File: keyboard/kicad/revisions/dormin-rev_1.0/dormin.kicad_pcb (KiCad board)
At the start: 2 copper layers, 141.5 x 103.1 mm, 24 parts

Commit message: feat: clean pcb and outline
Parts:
- added SW1: SW_Push, willkeebs_keyboard:SW_MX_Choc_Hotswap, F.Cu at (89.0, 76.8)
- added U3: XIAO-nRF52840-Plus-SMD, Seeed_Studio_XIAO_Series:XIAO-nRF52840-Plus-SMD, B.Cu at (194.0, 105.2)
- SW1: renamed from S6; value (none) -> SW_Push
- moved D23 68.7 mm to (78.8, 102.0)
- moved D24 68.7 mm to (83.4, 102.0)
- moved SW1 68.7 mm to (95.5, 105.3)
- moved SW11 68.7 mm to (95.5, 143.4)
- moved SW13 68.7 mm to (133.6, 133.9)
- moved SW14 68.7 mm to (152.6, 138.6)
- moved SW18 68.7 mm to (150.7, 163.4)
- moved SW3 68.7 mm to (133.6, 95.8)
- moved SW4 68.7 mm to (152.6, 100.5)
- moved SW6 68.7 mm to (95.5, 124.3)
- moved SW8 68.7 mm to (133.6, 114.8)
- moved SW9 68.7 mm to (152.6, 119.6)
- moved D21 68.7 mm to (69.4, 102.0)
- moved D22 68.7 mm to (74.1, 101.9)
- moved SW16 68.7 mm to (76.4, 114.8)
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- renumbered S17 to SW10, S4 to SW11, S7 to SW12, S10 to SW13, S13 to SW14, S16 to SW15, S3 to SW16, S2 to SW17, S19 to SW18, S20 to SW19, S9 to SW2, S21 to SW20, S12 to SW3, S15 to SW4, S18 to SW5, S5 to SW6, S8 to SW7, S11 to SW8, S14 to SW9
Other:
- outline, holes or cut-outs redrawn

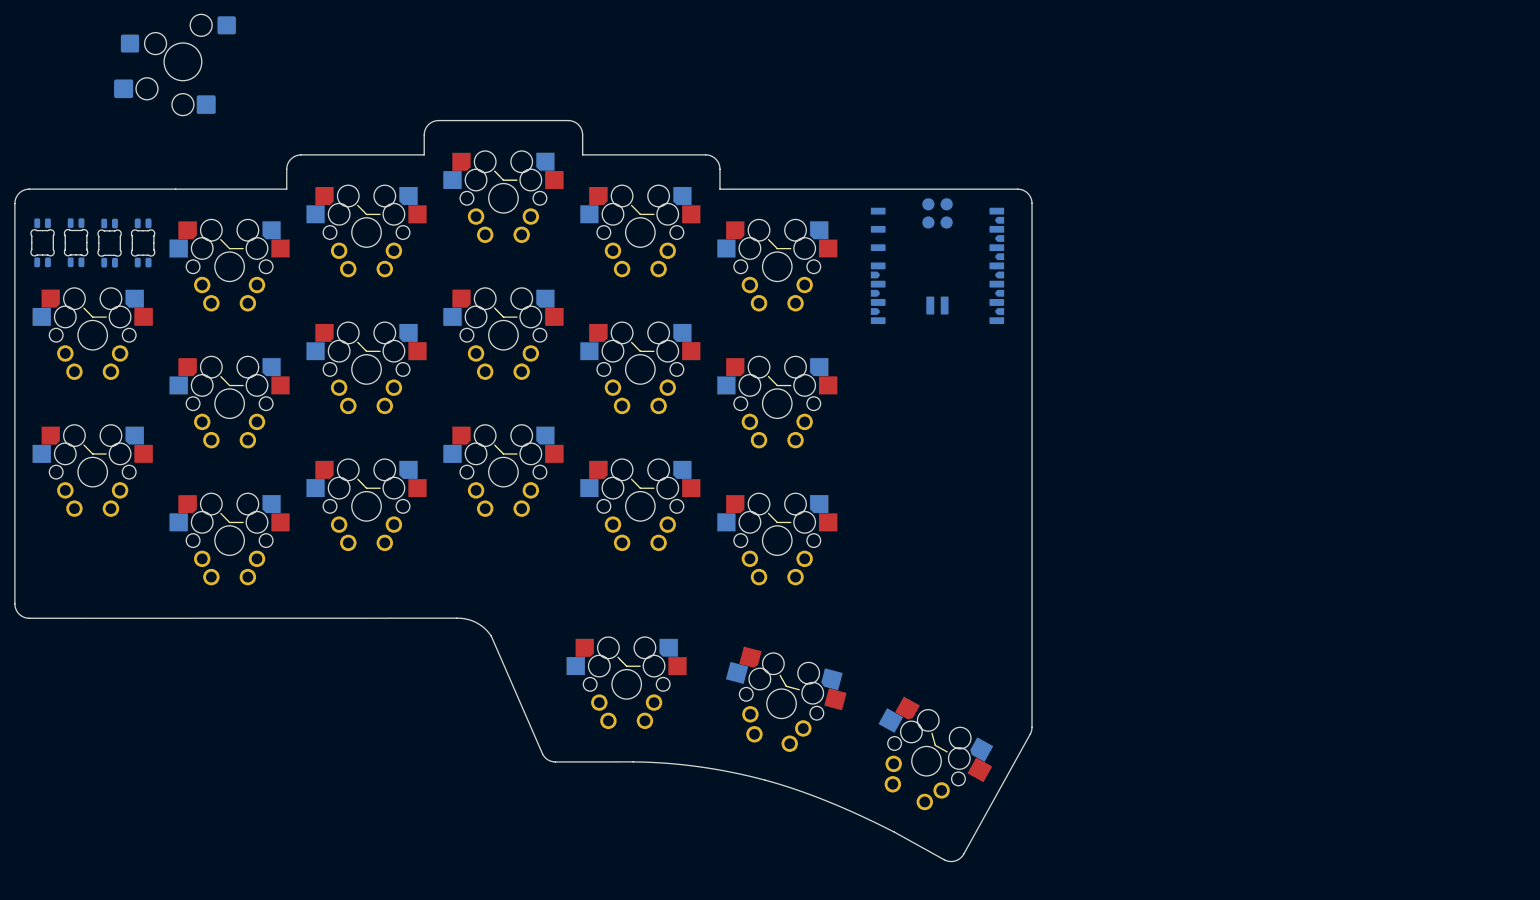
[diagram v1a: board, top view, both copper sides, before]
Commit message: feat: start PCB placement
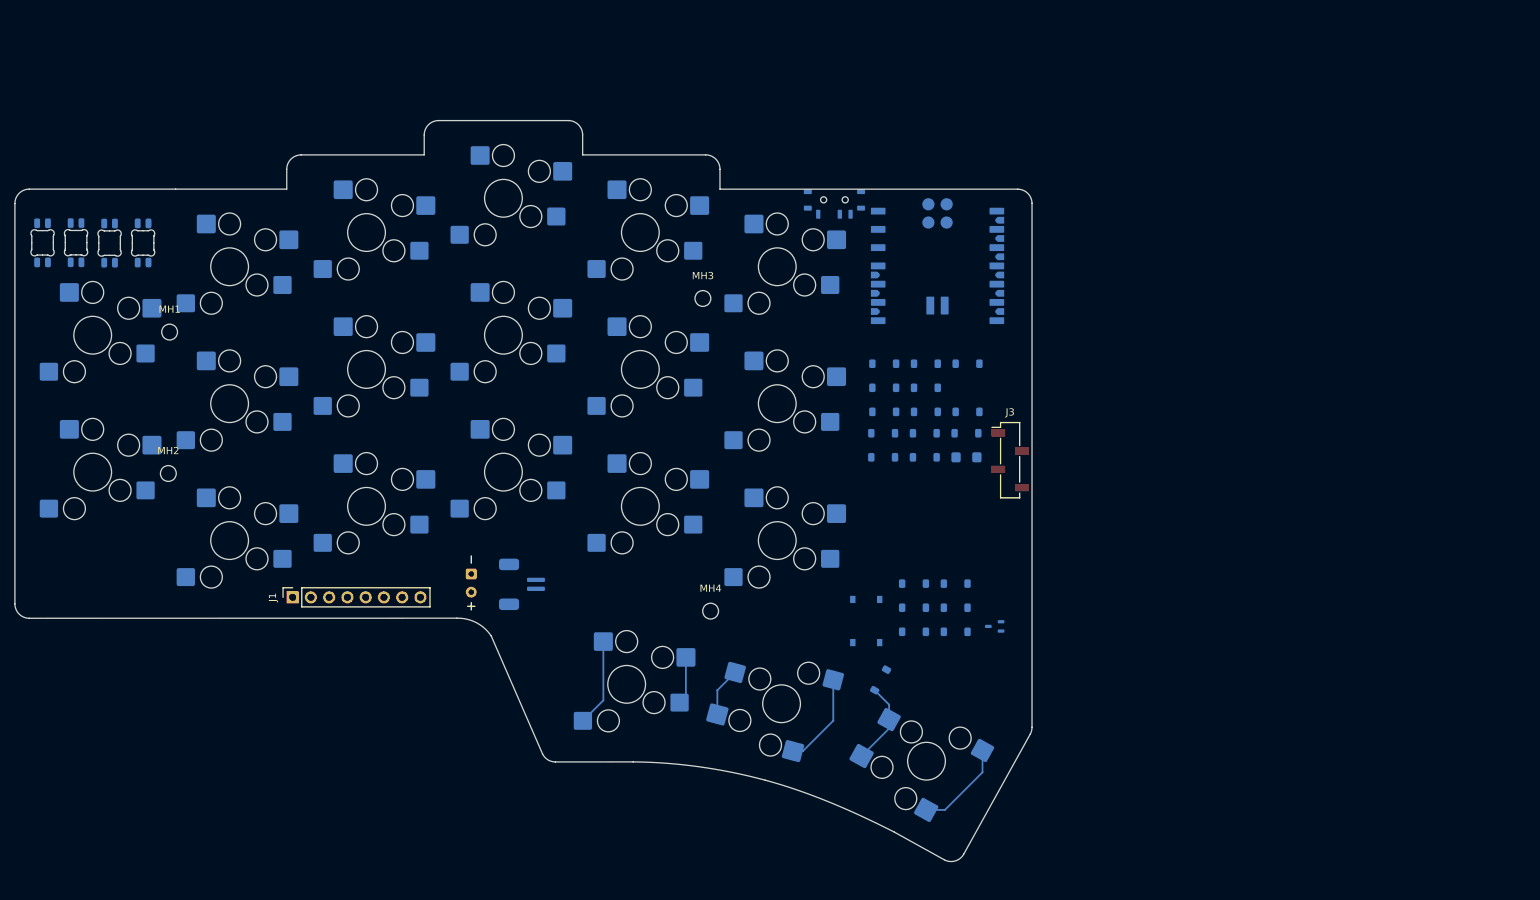
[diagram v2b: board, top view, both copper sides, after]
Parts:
- removed the SW1 at (89.0, 76.8)
- added BT1: Pads, willkeebs_power:Battery_Pad, F.Cu at (129.1, 149.3)
- added D1: 1N4148W, Diode_SMD:D_SOD-123, B.Cu at (186.6, 118.8)
- added D10: 1N4148W, Diode_SMD:D_SOD-123, B.Cu at (192.3, 122.1)
- added D11: 1N4148W, Diode_SMD:D_SOD-123, B.Cu at (192.3, 125.5)
- added D12: 1N4148W, Diode_SMD:D_SOD-123, B.Cu at (192.2, 128.4)
- added D13: 1N4148W, Diode_SMD:D_SOD-123, B.Cu at (192.2, 131.8)
- added D14: 1N4148W, Diode_SMD:D_SOD-123, B.Cu at (196.5, 149.4)
- added D15: 1N4148W, Diode_SMD:D_SOD-123, B.Cu at (196.5, 152.7)
- added D16: 1N4148W, Diode_SMD:D_SOD-123, B.Cu at (196.5, 156.1)
- added D17: 1N4148W, Diode_SMD:D_SOD-123, B.Cu at (198.1, 118.8)
- added D18: 1N4148W, Diode_SMD:D_SOD-123, B.Cu at (186.1, 162.8)
- added D19: 1N4148W, Diode_SMD:D_SOD-123, B.Cu at (198.1, 125.5)
- added D2: 1N4148W, Diode_SMD:D_SOD-123, B.Cu at (186.6, 122.1)
- added D20: 1N4148W, Diode_SMD:D_SOD-123, B.Cu at (198.0, 128.4)
- added D28: SMF5V0A, Diode_SMD:D_SMF, B.Cu at (198.0, 131.8)
- added D3: 1N4148W, Diode_SMD:D_SOD-123, B.Cu at (186.6, 125.5)
- added D4: 1N4148W, Diode_SMD:D_SOD-123, B.Cu at (186.4, 128.4)
- added D5: 1N4148W, Diode_SMD:D_SOD-123, B.Cu at (186.4, 131.8)
- added D6: 1N4148W, Diode_SMD:D_SOD-123, B.Cu at (190.7, 149.4)
- added D7: 1N4148W, Diode_SMD:D_SOD-123, B.Cu at (190.7, 152.7)
- added D8: 1N4148W, Diode_SMD:D_SOD-123, B.Cu at (190.7, 156.1)
- added D9: 1N4148W, Diode_SMD:D_SOD-123, B.Cu at (192.3, 118.8)
- added J1: Conn_01x08_Socket, Connector_PinSocket_2.54mm:PinSocket_1x08_P2.54mm_Vertical, F.Cu at (104.2, 151.3)
- added J3: Pogo Connector, Connector_PinSocket_2.54mm:PinSocket_1x04_P2.54mm_Vertical_SMD_Pin1Left, F.Cu at (204.1, 132.2)
- added JST1: Conn_01x02_Pin, willkeebs_power:JST_1.25mm, B.Cu at (135.6, 149.5)
- added MH1: MountingHole_2.2mm_M2, MountingHole:MountingHole_2.2mm_M2, F.Cu at (87.1, 114.4)
- added MH2: MountingHole_2.2mm_M2, MountingHole:MountingHole_2.2mm_M2, F.Cu at (87.0, 134.1)
- added MH3: MountingHole_2.2mm_M2, MountingHole:MountingHole_2.2mm_M2, F.Cu at (161.3, 109.7)
- added MH4: MountingHole_2.2mm_M2, MountingHole:MountingHole_2.2mm_M2, F.Cu at (162.4, 153.2)
- added PSW1: SW_SPDT, willkeebs_power:Switch_MSK12C02, B.Cu at (179.6, 96.0)
- added RSW1: SW_Push, willkeebs_components:SW_Push_1P1T_XKB_TS-1187A, B.Cu at (184.1, 154.6)
- added U4: TPD2E2U06DCK, Package_TO_SOT_SMD:SOT-323_SC-70, B.Cu at (201.9, 155.3)
- SW1: renamed from SW5; value (none) -> SW_Push; footprint ceoloide:switch_mx -> willkeebs_keyboard:SW_MX_Choc_Hotswap; moved to F.Cu
- SW10: renamed from SW6; value (none) -> SW_Push; footprint ceoloide:switch_mx -> willkeebs_keyboard:SW_MX_Choc_Hotswap; moved to F.Cu
- SW11: renamed from SW16; value (none) -> SW_Push; footprint ceoloide:switch_mx -> willkeebs_keyboard:SW_MX_Choc_Hotswap; moved to F.Cu
- SW12: renamed from SW15; value (none) -> SW_Push; footprint ceoloide:switch_mx -> willkeebs_keyboard:SW_MX_Choc_Hotswap; moved to F.Cu
- SW13: renamed from SW14; value (none) -> SW_Push; footprint ceoloide:switch_mx -> willkeebs_keyboard:SW_MX_Choc_Hotswap; moved to F.Cu
- SW14: renamed from SW13; value (none) -> SW_Push; footprint ceoloide:switch_mx -> willkeebs_keyboard:SW_MX_Choc_Hotswap; moved to F.Cu
- SW15: renamed from SW12; value (none) -> SW_Push; footprint ceoloide:switch_mx -> willkeebs_keyboard:SW_MX_Choc_Hotswap; moved to F.Cu
- SW16: renamed from SW11; value (none) -> SW_Push; footprint ceoloide:switch_mx -> willkeebs_keyboard:SW_MX_Choc_Hotswap; moved to F.Cu
- SW17, SW19, SW3, SW8: value (none) -> SW_Push; footprint ceoloide:switch_mx -> willkeebs_keyboard:SW_MX_Choc_Hotswap; moved to F.Cu
- SW18: renamed from SW20; value (none) -> SW_Push; footprint ceoloide:switch_mx -> willkeebs_keyboard:SW_MX_Choc_Hotswap; moved to F.Cu
- SW2: renamed from SW4; value (none) -> SW_Push; footprint ceoloide:switch_mx -> willkeebs_keyboard:SW_MX_Choc_Hotswap; moved to F.Cu
- SW20: renamed from SW18; value (none) -> SW_Push; footprint ceoloide:switch_mx -> willkeebs_keyboard:SW_MX_Choc_Hotswap; moved to F.Cu
- SW4: renamed from SW2; value (none) -> SW_Push; footprint ceoloide:switch_mx -> willkeebs_keyboard:SW_MX_Choc_Hotswap; moved to F.Cu
- SW5: renamed from SW1; footprint ceoloide:switch_mx -> willkeebs_keyboard:SW_MX_Choc_Hotswap; moved to F.Cu
- SW6: renamed from SW10; value (none) -> SW_Push; footprint ceoloide:switch_mx -> willkeebs_keyboard:SW_MX_Choc_Hotswap; moved to F.Cu
- SW7: renamed from SW9; value (none) -> SW_Push; footprint ceoloide:switch_mx -> willkeebs_keyboard:SW_MX_Choc_Hotswap; moved to F.Cu
- SW9: renamed from SW7; value (none) -> SW_Push; footprint ceoloide:switch_mx -> willkeebs_keyboard:SW_MX_Choc_Hotswap; moved to F.Cu
- turned SW1 to 180 degrees
- turned SW10 to 180 degrees
- turned SW11 to 180 degrees
- turned SW12 to 180 degrees
- turned SW13 to 180 degrees
- turned SW14 to 180 degrees
- turned SW15 to 180 degrees
- turned SW16 to 180 degrees
- turned SW17 to 180 degrees
- turned SW2 to 180 degrees
- turned SW20 to 180 degrees
- turned SW3 to 180 degrees
- turned SW4 to 180 degrees
- turned SW5 to 180 degrees
- turned SW6 to 180 degrees
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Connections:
- SW1 pad 1: (no net) -> Net-(D1-A)
- SW1 pad 2: inner_top_sw -> COL5
- SW10 pad 1: (no net) -> Net-(D10-A)
- SW10 pad 2: pinky_home_sw -> COL1
- SW11 pad 1: (no net) -> Net-(D11-A)
- SW11 pad 2: outer_top_sw -> COL0
- SW12 pad 1: (no net) -> Net-(D12-A)
- SW12 pad 2: inner_bottom_sw -> COL5
- SW13 pad 1: (no net) -> Net-(D13-A)
- SW13 pad 2: index_bottom_sw -> COL4
- SW14 pad 1: (no net) -> Net-(D14-A)
- SW14 pad 2: middle_bottom_sw -> COL3
- SW15 pad 1: (no net) -> Net-(D15-A)
- SW15 pad 2: ring_bottom_sw -> COL2
- SW16 pad 1: (no net) -> Net-(D16-A)
- SW16 pad 2: pinky_bottom_sw -> COL1
- SW17 pad 1: (no net) -> Net-(D17-A)
- SW17 pad 2: outer_home_sw -> COL0
- SW18 pad 1: (no net) -> Net-(D18-A)
- SW18 pad 2: outer_only_sw -> COL5
- SW19 pad 1: (no net) -> Net-(D19-A)
- SW19 pad 2: home_only_sw -> COL4
- SW2 pad 1: (no net) -> Net-(D2-A)
- SW2 pad 2: index_top_sw -> COL4
- SW20 pad 1: (no net) -> Net-(D20-A)
- SW20 pad 2: inner_only_sw -> COL3
- SW3 pad 1: (no net) -> Net-(D3-A)
- SW3 pad 2: middle_top_sw -> COL3
- SW4 pad 1: (no net) -> Net-(D4-A)
- SW4 pad 2: ring_top_sw -> COL2
- SW5 pad 1: (no net) -> Net-(D5-A)
- SW5 pad 2: pinky_top_sw -> COL1
- SW6 pad 1: (no net) -> Net-(D6-A)
- SW6 pad 2: inner_home_sw -> COL5
- SW7 pad 1: (no net) -> Net-(D7-A)
- SW7 pad 2: index_home_sw -> COL4
- SW8 pad 1: (no net) -> Net-(D8-A)
- SW8 pad 2: middle_home_sw -> COL3
- SW9 pad 1: (no net) -> Net-(D9-A)
- SW9 pad 2: ring_home_sw -> COL2
- U3 pad 19: EXTG -> unconnected-(U3-D15_NFC2-Pad19)
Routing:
- net COL4: track 0.00 -> 13.0 mm
- net COL5: track 0.00 -> 13.0 mm
- net COL3: track 0.00 -> 12.2 mm
- net Net-(D18-A): track 0.00 -> 11.6 mm
- net Net-(D19-A): track 0.00 -> 6.88 mm
- net Net-(D20-A): track 0.00 -> 6.66 mm

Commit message: feat: added pogo-pin pcb components
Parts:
- removed J1: Conn_01x08_Socket, Connector_PinSocket_2.54mm:PinSocket_1x08_P2.54mm_Vertical
- added D27: D_Schottky, Diode_SMD:Nexperia_CFP3_SOD-123W, B.Cu at (199.0, 118.4)
- added F2: Polyfuse, Fuse:Fuse_1206_3216Metric, B.Cu at (196.4, 118.4)
- added R5: 33R, Resistor_SMD:R_0402_1005Metric, B.Cu at (192.7, 117.0)
- added R6: 33R, Resistor_SMD:R_0402_1005Metric, B.Cu at (194.2, 117.0)
- J3: moved to B.Cu
- moved D17 130.1 mm to (70.8, 145.3), turned to -90 degrees
- moved D11 123.2 mm to (69.2, 124.0), turned to -90 degrees
- moved D16 110.1 mm to (86.8, 146.0), turned to -90 degrees
- moved D10 105.6 mm to (86.8, 123.0), turned to -90 degrees
- moved D15 91.2 mm to (105.7, 143.9), turned to -90 degrees
- moved D9 86.8 mm to (105.9, 127.1), turned to -90 degrees
- moved D4 86.5 mm to (106.2, 95.8), turned to -90 degrees
- moved D5 83.7 mm to (105.0, 112.3), turned to -90 degrees
- moved D8 77.1 mm to (125.1, 115.5), turned to -90 degrees
- moved D14 73.3 mm to (125.3, 131.9), turned to -90 degrees
- moved D3 70.2 mm to (125.4, 91.1), turned to -90 degrees
- moved D20 64.4 mm to (141.3, 159.0), turned to -90 degrees
- moved D7 59.7 mm to (144.6, 114.8), turned to -90 degrees
- moved D2 49.3 mm to (144.8, 95.9), turned to -90 degrees
- moved D19 48.3 mm to (163.1, 158.7), turned to -105 degrees
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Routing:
- net Net-(BT1-+): track 0.00 -> 102.9 mm
- net Net-(J3-Pin_3): track 0.00 -> 39.2 mm, vias 0 -> 4
- net USB_VBUS: track 0.00 -> 30.7 mm
- net Net-(D27-K): track 0.00 -> 26.4 mm
- net BAT+: track 0.00 -> 24.5 mm
- net EXTC: track 0.00 -> 20.5 mm, vias 0 -> 2
- net EXTE: track 0.00 -> 15.3 mm, vias 0 -> 2
- net GND: track 0.00 -> 5.54 mm, vias 0 -> 3
- net Net-(D27-A): track 0.00 -> 3.89 mm
- net Net-(J3-Pin_4): track 0.00 -> 3.34 mm

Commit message: feat: added support for white backlight (wip)
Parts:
- added C1: 100nF, Capacitor_SMD:C_0603_1608Metric, B.Cu at (186.0, 128.0)
- added C2: 10uF, Capacitor_SMD:C_0603_1608Metric, B.Cu at (188.1, 128.0)
- added D25: LED, willkeebs_components:LED_MHT151WDT, B.Cu at (171.3, 100.1)
- added D26: LED, willkeebs_components:LED_MHT151WDT, B.Cu at (152.3, 94.8)
- added D29: LED, willkeebs_components:LED_MHT151WDT, B.Cu at (133.2, 90.3)
- added D30: LED, willkeebs_components:LED_MHT151WDT, B.Cu at (114.2, 95.0)
- added D31: LED, willkeebs_components:LED_MHT151WDT, B.Cu at (95.4, 100.2)
- added D32: LED, willkeebs_components:LED_MHT151WDT, B.Cu at (171.6, 118.9)
- added D33: LED, willkeebs_components:LED_MHT151WDT, B.Cu at (152.3, 114.1)
- added D34: LED, willkeebs_components:LED_MHT151WDT, B.Cu at (133.0, 109.3)
- added D35: LED, willkeebs_components:LED_MHT151WDT, B.Cu at (114.3, 114.3)
- added D36: LED, willkeebs_components:LED_MHT151WDT, B.Cu at (95.4, 118.8)
- added D37: LED, willkeebs_components:LED_MHT151WDT, B.Cu at (76.0, 109.3)
- added D38: LED, willkeebs_components:LED_MHT151WDT, B.Cu at (171.3, 138.1)
- added D39: LED, willkeebs_components:LED_MHT151WDT, B.Cu at (152.2, 133.3)
- added D40: LED, willkeebs_components:LED_MHT151WDT, B.Cu at (133.2, 128.7)
- added D41: LED, willkeebs_components:LED_MHT151WDT, B.Cu at (114.4, 133.2)
- added D42: LED, willkeebs_components:LED_MHT151WDT, B.Cu at (95.3, 138.2)
- added D43: LED, willkeebs_components:LED_MHT151WDT, B.Cu at (76.5, 128.5)
- added D44: LED, willkeebs_components:LED_MHT151WDT, B.Cu at (150.4, 158.1)
- added D45: LED, willkeebs_components:LED_MHT151WDT, B.Cu at (173.4, 160.9)
- added D46: LED, willkeebs_components:LED_MHT151WDT, B.Cu at (194.8, 169.3)
- added Q1: HX2302A, Package_TO_SOT_SMD:SOT-23, B.Cu at (185.3, 133.8)
- added R1: 1K, Resistor_SMD:R_0603_1608Metric, B.Cu at (175.7, 100.1)
- added R10: 1K, Resistor_SMD:R_0603_1608Metric, B.Cu at (138.2, 109.9)
- added R11: 1K, Resistor_SMD:R_0603_1608Metric, B.Cu at (119.3, 114.7)
- added R12: 1K, Resistor_SMD:R_0603_1608Metric, B.Cu at (100.2, 119.2)
- added R13: 1K, Resistor_SMD:R_0603_1608Metric, B.Cu at (81.2, 109.9)
- added R14: 1K, Resistor_SMD:R_0603_1608Metric, B.Cu at (176.2, 138.2)
- added R15: 1K, Resistor_SMD:R_0603_1608Metric, B.Cu at (157.5, 133.9)
- added R16: 1K, Resistor_SMD:R_0603_1608Metric, B.Cu at (138.6, 129.0)
- added R17: 1K, Resistor_SMD:R_0603_1608Metric, B.Cu at (119.5, 133.9)
- added R18: 1K, Resistor_SMD:R_0603_1608Metric, B.Cu at (100.3, 138.4)
- added R19: 1K, Resistor_SMD:R_0603_1608Metric, B.Cu at (81.5, 129.1)
- added R2: 1K, Resistor_SMD:R_0603_1608Metric, B.Cu at (157.2, 95.4)
- added R20: 1K, Resistor_SMD:R_0603_1608Metric, B.Cu at (155.4, 158.4)
- added R21: 1K, Resistor_SMD:R_0603_1608Metric, B.Cu at (178.2, 162.4)
- added R22: 1K, Resistor_SMD:R_0603_1608Metric, B.Cu at (199.3, 171.9)
- added R3: 1K, Resistor_SMD:R_0603_1608Metric, B.Cu at (138.4, 90.8)
- added R4: 1K, Resistor_SMD:R_0603_1608Metric, B.Cu at (119.2, 95.4)
- added R7: 1K, Resistor_SMD:R_0603_1608Metric, B.Cu at (100.4, 100.2)
- added R706: 100R, Resistor_SMD:R_0603_1608Metric, B.Cu at (188.9, 132.0)
- added R707: 10k, Resistor_SMD:R_0603_1608Metric, B.Cu at (188.9, 136.4)
- added R8: 1K, Resistor_SMD:R_0603_1608Metric, B.Cu at (176.6, 119.2)
- added R9: 1K, Resistor_SMD:R_0603_1608Metric, B.Cu at (157.6, 114.6)
- SW1, SW10, SW11, SW12, SW13, SW14, SW15, SW16, SW17, SW18, SW19, SW2, SW20, SW3, SW4, SW5, SW6, SW7, SW8, SW9: footprint willkeebs_keyboard:SW_MX_Choc_Hotswap -> willkeebs_keyboard:NF_LED_1206_SW_KS33_3_0_HS_1U
- moved PSW1 39.7 mm to (205.4, 126.2), turned to 90 degrees
- moved RSW1 7.40 mm to (177.7, 153.9), turned to 0 degrees
- moved D1 0.89 mm to (165.4, 100.0), turned to 0 degrees
- moved D6 0.79 mm to (165.6, 119.2), turned to 0 degrees
- moved BT1 0.16 mm to (129.1, 149.5), turned to -90 degrees
- turned SW18 to 151 degrees
- turned SW19 to 165 degrees
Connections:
- net USB_VBUS renamed 5V
- net VCC renamed 3V3
- JST1 pad 1: GND -> Net-(BT1-+)
- JST1 pad 2: Net-(BT1-+) -> GND
- PSW1 pad 2: BAT+ -> Net-(BT1-+)
- PSW1 pad 3: Net-(BT1-+) -> BAT+
- U3 pad 19: unconnected-(U3-D15_NFC2-Pad19) -> LED_PWM
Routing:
- net Net-(BT1-+): track 102.9 -> 55.1 mm
- net BAT+: track 24.5 -> 0.00 mm
- net GND: track 5.54 -> 19.8 mm, vias 3 -> 4
- net Net-(D19-A): track 6.88 -> 19.9 mm
- net COL4: track 13.0 -> 0.00 mm
- net Net-(D18-A): track 11.6 -> 24.6 mm
- net COL5: track 13.0 -> 0.00 mm
- net Net-(D1-A): track 0.00 -> 1.25 mm
